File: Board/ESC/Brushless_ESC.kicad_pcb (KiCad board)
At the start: 2 copper layers, 63 x 36 mm, 77 parts, among them IC1 ATMEGA88PA-A, P1 Battery+, P2 Battery-, P3 Coil_A, P4 PPM, P5 Coil_B, P6 Coil_C, P7 I2C, P8 ISP, Q1 IRL7843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

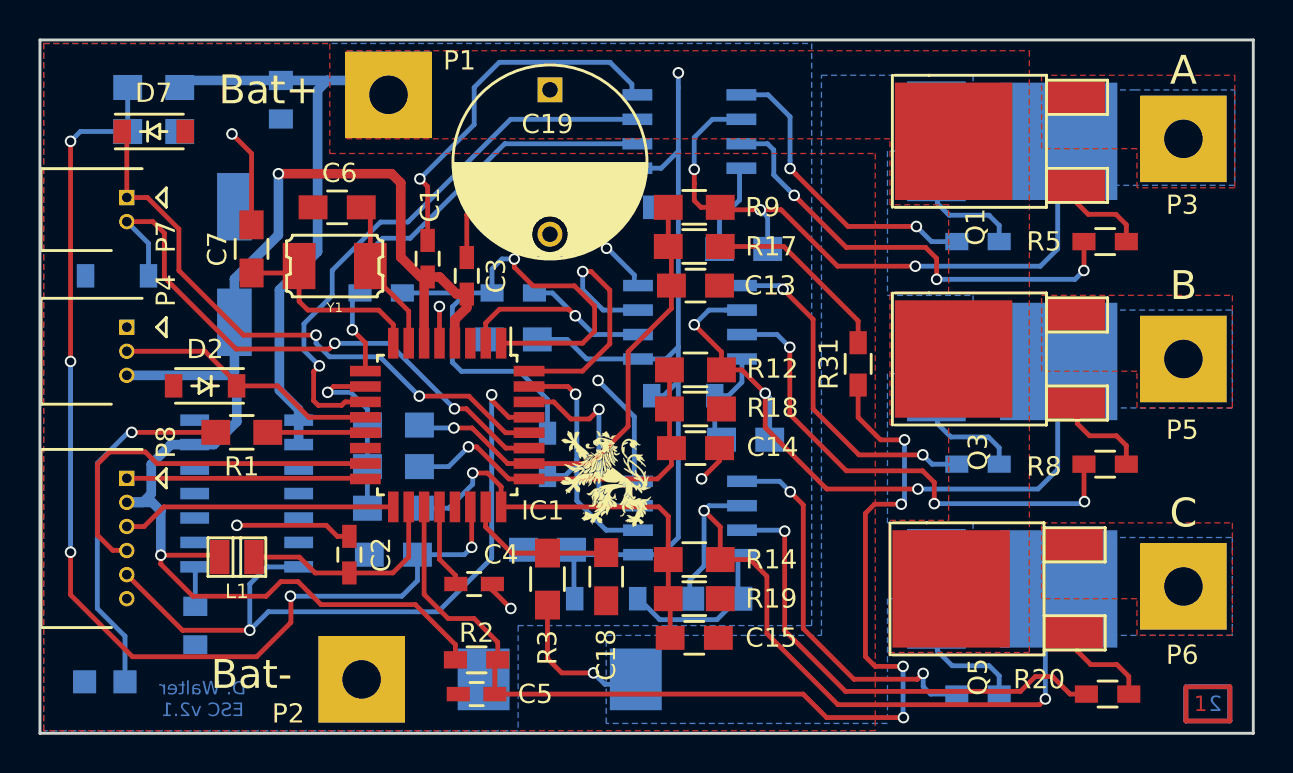
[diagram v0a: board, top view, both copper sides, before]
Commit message: Fixed 3d Models
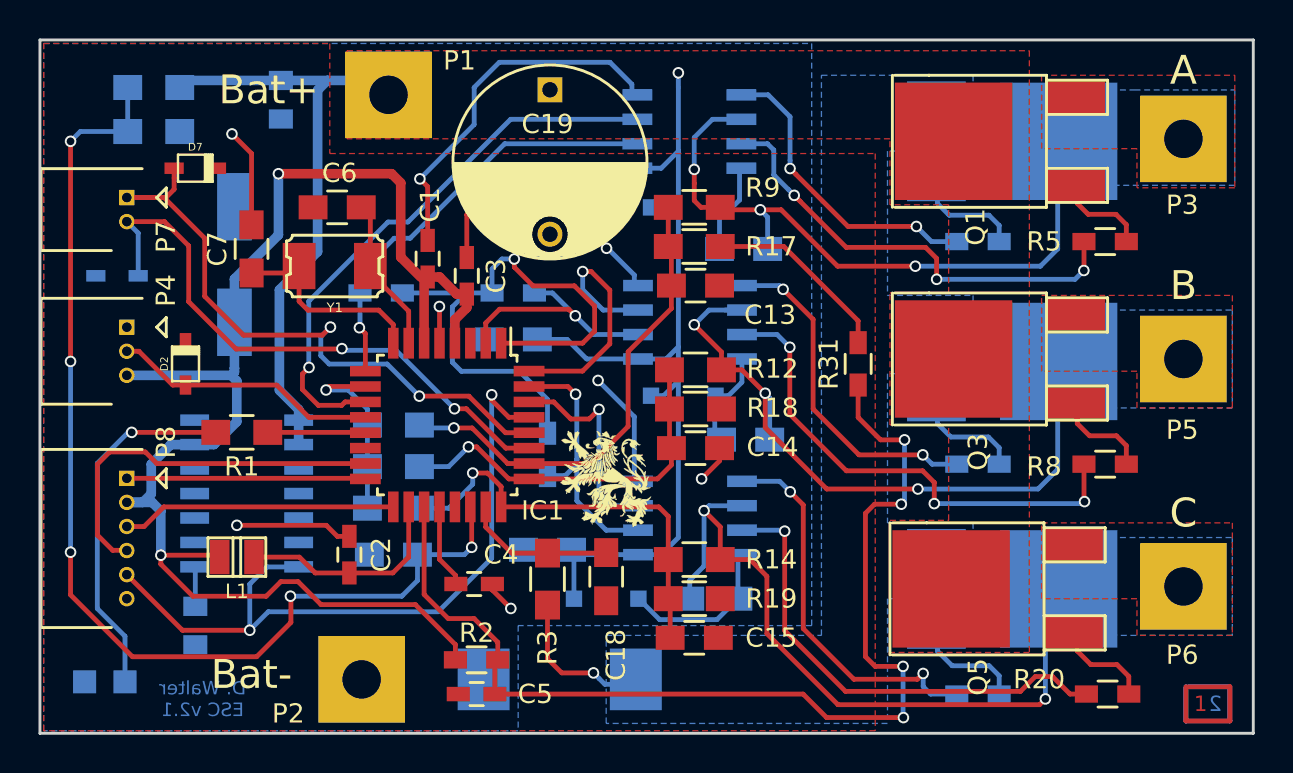
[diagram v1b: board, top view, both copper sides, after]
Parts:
- D1: footprint LEDs:LED-0805 -> LEDs:LED_0805
- D2, D3, D7: footprint Diodes_SMD:SOD-123 -> w_smd_diode:sod323
- D4, D5, D6: footprint Diodes_SMD:SOD-123 -> w_smd_diode:sod123
- moved D7 2.88 mm to (124.4, 65.7)
- moved D2 1.53 mm to (123.9, 75.8), turned to 90 degrees
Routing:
- net /Controller/SCL: track 31.0 -> 33.4 mm
- net /Controller/IN_A: track 22.8 -> 22.2 mm

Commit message: Minor Layout changes
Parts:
- D7: moved to B.Cu
- moved D6 4.33 mm to (150.1, 87.8)
- moved C16 3.94 mm to (155.1, 87.0), turned to 90 degrees
- moved D7 2.27 mm to (123.4, 67.7), turned to 270 degrees
- moved D2 2.05 mm to (122.9, 74.0)
- moved R21 1.92 mm to (142.4, 78.6)
- moved D3 1.78 mm to (122.1, 71.2), turned to 0 degrees
- moved R20 1.65 mm to (170.1, 93.0)
- moved R5 1.52 mm to (170.1, 69.5)
- moved R8 1.52 mm to (170.1, 81.0)
- moved C10 0.80 mm to (143.4, 85.7)
- moved C6 0.76 mm to (131.8, 68.5)
- moved Y1 0.76 mm to (131.6, 71.5)
- moved C7 0.64 mm to (127.3, 70.5)
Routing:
- net GND: track 57.7 -> 65.9 mm, vias 9 -> 15
- net /Controller/Reset: track 38.1 -> 35.2 mm
- net /Controller/SCL: track 33.4 -> 31.2 mm
- net /Controller/IN_C: track 14.1 -> 15.9 mm
- net Net-(Q1-Pad1): track 4.93 -> 3.38 mm
- net +5V: track 75.9 -> 74.3 mm
- net Net-(Q5-Pad1): track 5.19 -> 3.68 mm
- net Net-(R20-Pad2): track 25.1 -> 23.6 mm
- net Net-(Q3-Pad1): track 5.03 -> 3.64 mm
- net Net-(R5-Pad2): track 24.1 -> 22.9 mm
- net /Controller/PWM: track 30.6 -> 29.3 mm
- net Net-(Q2-Pad1): track 5.57 -> 6.70 mm
- net Net-(Q4-Pad1): track 5.63 -> 6.76 mm
- net +BATT: track 82.5 -> 83.5 mm
- net Net-(C16-Pad1): track 8.44 -> 7.38 mm
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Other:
- board text added: "5V"
- board text added: "GND"
- board text added: "I2C"
- board text added: "ISP"
- board text added: "PPM"
- board text added: "SCL"
- board text added: "SDA"

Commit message: Some more Layout changes, Layout now Final
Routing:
- net (no net): track 16.0 -> 0.00 mm
- net /Power/Coil_B: track 36.3 -> 35.4 mm

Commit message: Some more Layout changes, Layout now Final
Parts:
- C20, C22: footprint Capacitors_SMD:C_0805 -> Capacitors_SMD:C_0805_HandSoldering
- D2, D3, D7: value ZENER -> ZD5,6; footprint w_smd_diode:sod323 -> w_smd_trans:sot23
- moved D7 5.37 mm to (119.3, 71.2), turned to 0 degrees
- moved D2 2.32 mm to (124.4, 75.8), turned to 270 degrees
- moved D3 0.70 mm to (122.8, 71.2)
- moved C22 0.64 mm to (124.4, 90.0)
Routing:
- net /Controller/SCL: track 31.2 -> 32.5 mm
- net /Controller/PPM: track 13.9 -> 14.8 mm
- net /Controller/V_Bat: track 57.2 -> 56.3 mm
- net /Controller/SDA: track 31.6 -> 30.8 mm
